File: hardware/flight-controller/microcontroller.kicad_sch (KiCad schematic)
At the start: 40 parts, among them J1 IDC-6, J2 IDC-10, J3 Conn_01x05, SW1 SW_Push, U1 STM32U535RET6, U2 ESP-12E, Y1 8 MHz

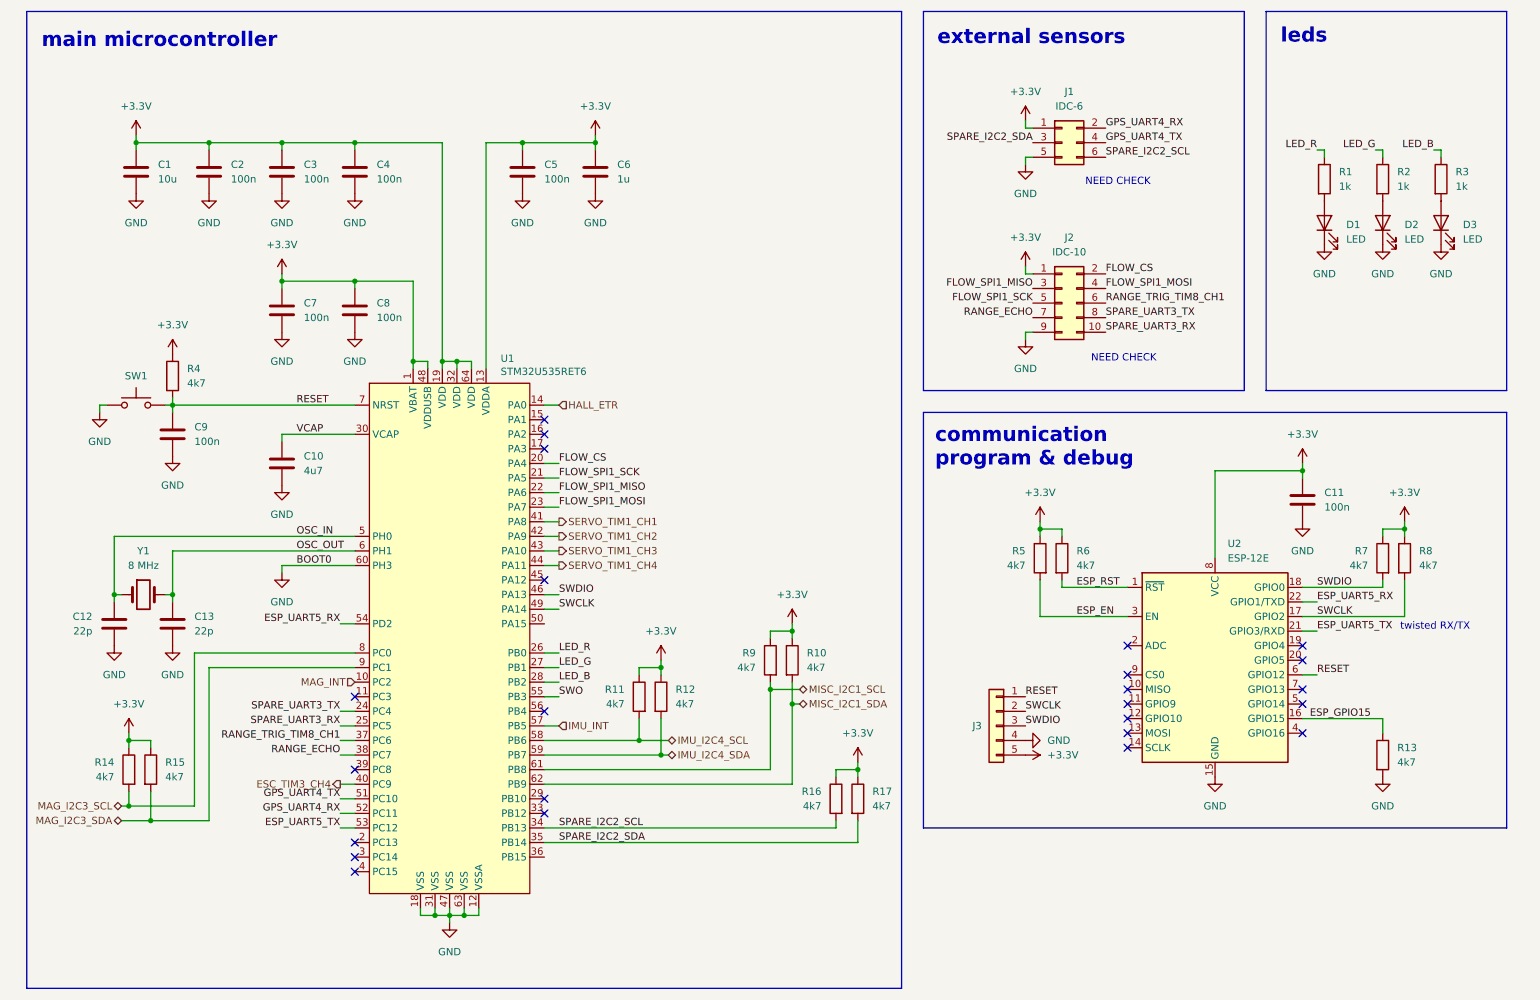
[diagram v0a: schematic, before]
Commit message: sensors, power, actuators, filters
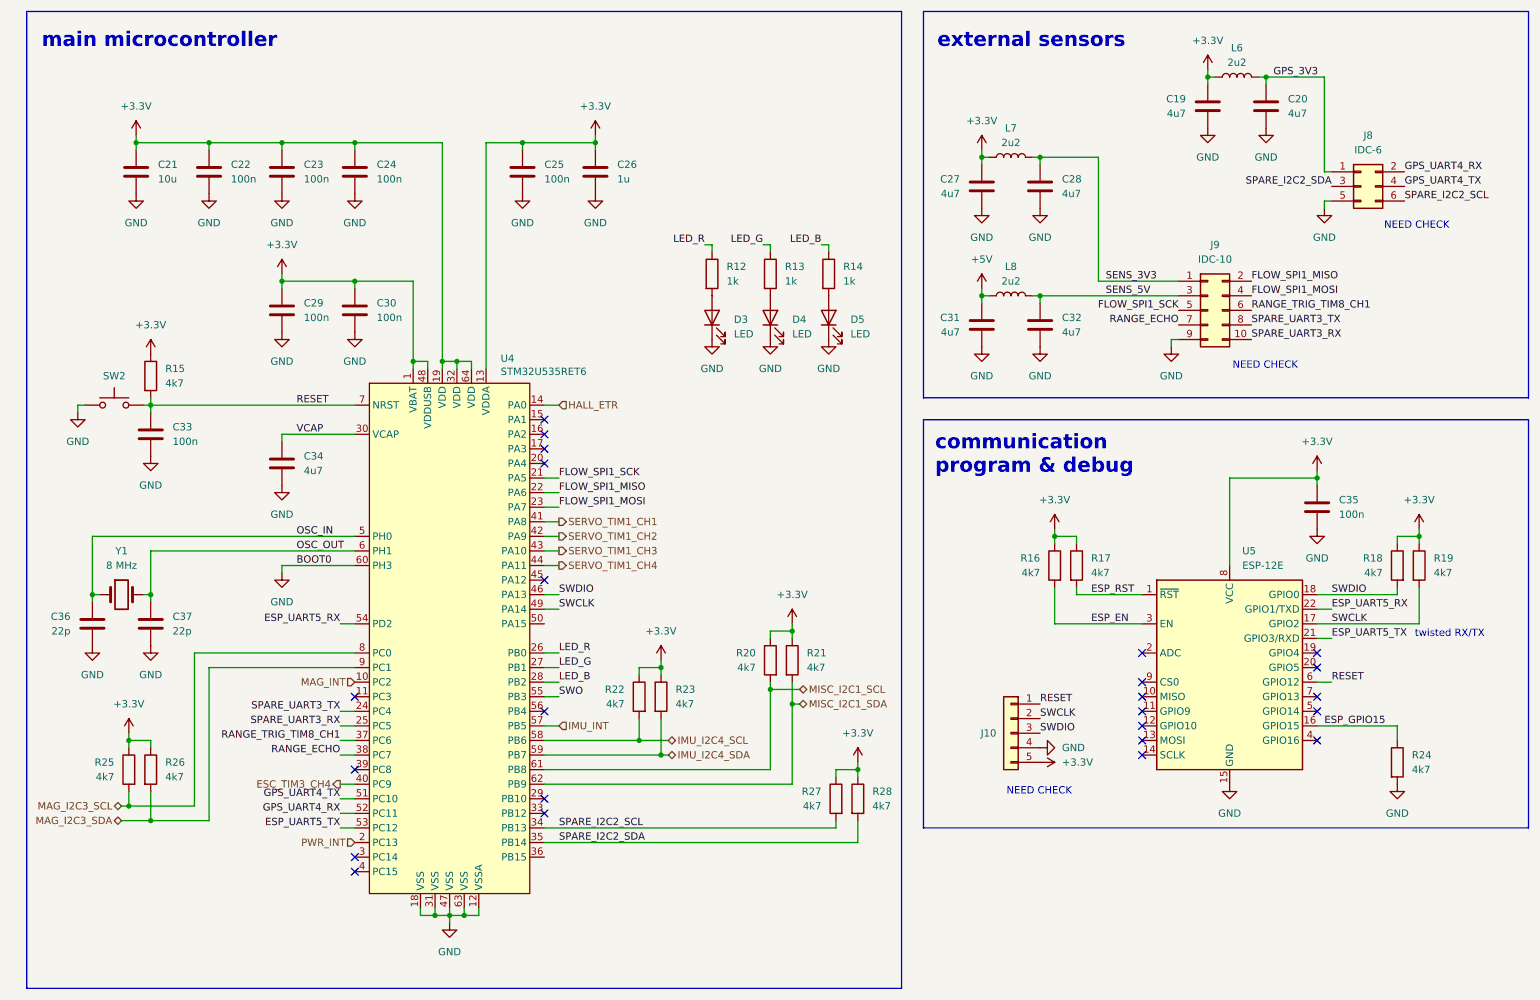
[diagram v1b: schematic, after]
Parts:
- removed C11: 100n, symbol Device:C
- added C19, C20, C27, C28, C31, C32: 4u7, symbol Device:C
- added C35: 100n, symbol Device:C
- added L6, L7, L8: 2u2, symbol Device:L
- renumbered C1 to C21, C2 to C22, C3 to C23, C4 to C24, C5 to C25, C6 to C26, C7 to C29, C8 to C30, C9 to C33, C10 to C34, C12 to C36, C13 to C37, D1 to D3, D2 to D4, D3 to D5, J3 to J10, J1 to J8, J2 to J9, R1 to R12, R2 to R13, R3 to R14, R4 to R15, R5 to R16, R6 to R17, R7 to R18, R8 to R19, R9 to R20, R10 to R21, R11 to R22, R12 to R23, R13 to R24, R14 to R25, R15 to R26, R16 to R27, R17 to R28, SW1 to SW2, U1 to U4, U2 to U5
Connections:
- net +3.3V: now also C19.1, C27.1, C35.1, L6.1, L7.1; no longer J8.1 (Pin_1), J9.1 (Pin_1)
- net FLOW_SPI1_MISO: now also J9.2 (Pin_2); no longer J9.3 (Pin_3)
- net GND: now also C19.2, C20.2, C27.2, C28.2, C31.2, C32.2, C35.2
- net PWR_INT: now reaches U4.2 (PC13)
- net FLOW_CS: no longer names the net of U4.20 (PA4)
- net FLOW_CS: no longer J9.2 (Pin_2)
- new net +5V: C31.1, L8.1
- new net GPS_3V3: C20.1, J8.1 (Pin_1), L6.2
- new net SENS_3V3: C28.1, J9.1 (Pin_1), L7.2
- new net SENS_5V: C32.1, J9.3 (Pin_3), L8.2
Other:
- note removed: "leds"
- moved on the sheet: C33, C36, C37, D3, D4, D5, J10, J8, J9, R12, R13, R14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

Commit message: schematic cleanup
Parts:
- removed C19, C20, C27, C28, C31, C32: 4u7, symbol Device:C
- removed J8: IDC-6, symbol Connector_Generic:Conn_02x03_Odd_Even
- removed J9: IDC-10, symbol Connector_Generic:Conn_02x05_Odd_Even
- removed L6, L7, L8: 2u2, symbol Device:L
- removed R27, R28: 4k7, symbol Device:R
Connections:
- net FLOW_CS: now reaches U4.20 (PA4)
- net ESC_TIM3_CH4 renamed ESC
- net ESP_UART5_RX renamed ESP_RX
- net ESP_UART5_TX renamed ESP_TX
- net FLOW_SPI1_MISO renamed FLOW_MISO
- net FLOW_SPI1_MOSI renamed FLOW_MOSI
- net FLOW_SPI1_SCK renamed FLOW_SCK
- net GPS_UART4_RX renamed GPS_RX
- net GPS_UART4_TX renamed GPS_TX
- net HALL_ETR renamed HALL
- net IMU_I2C4_SCL renamed IMU_SCL
- net IMU_I2C4_SDA renamed IMU_SDA
- net MAG_I2C3_SCL renamed MAG_SCL
- net MAG_I2C3_SDA renamed MAG_SDA
- net MISC_I2C1_SCL renamed MISC_SCL
- net MISC_I2C1_SDA renamed MISC_SDA
- net RANGE_TRIG_TIM8_CH1 renamed RANGE_TRIG
- net SERVO_TIM1_CH1 renamed SERVO1
- net SERVO_TIM1_CH2 renamed SERVO2
- net SERVO_TIM1_CH3 renamed SERVO3
- net SERVO_TIM1_CH4 renamed SERVO4
- net SPARE_I2C2_SCL: no longer names the net of U4.34 (PB13)
- net SPARE_I2C2_SDA: no longer names the net of U4.35 (PB14)
- net SPARE_UART3_RX: no longer names the net of U4.25 (PC5)
- net SPARE_UART3_TX renamed FLOW_INT
- no-connect marks 24 -> 28
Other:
- note added: "twisted"
- note removed: "external sensors"
- note removed: "twisted RX/TX"
- moved on the sheet: C35, J10, R16, R17, R18, R19, R24, U5

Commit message: still working
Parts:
- removed R12, R13, R14: 1k, symbol Device:R
- removed R22, R23, R25, R26: 4k7, symbol Device:R
- added R18, R19, R20: 1k, Resistor_SMD:R_0603_1608Metric, symbol Device:R
- C12: renamed from C22; footprint (none) -> Capacitor_SMD:C_0603_1608Metric
- C13: renamed from C23; footprint (none) -> Capacitor_SMD:C_0603_1608Metric
- C14: renamed from C24; footprint (none) -> Capacitor_SMD:C_0603_1608Metric
- C15: renamed from C25; footprint (none) -> Capacitor_SMD:C_0603_1608Metric
- C17: renamed from C35; footprint (none) -> Capacitor_SMD:C_0603_1608Metric
- C18: renamed from C29; footprint (none) -> Capacitor_SMD:C_0603_1608Metric
- C19: renamed from C30; footprint (none) -> Capacitor_SMD:C_0603_1608Metric
- C20: renamed from C33; footprint (none) -> Capacitor_SMD:C_0603_1608Metric
- C22: renamed from C36; footprint (none) -> Capacitor_SMD:C_0603_1608Metric
- C23: renamed from C37; footprint (none) -> Capacitor_SMD:C_0603_1608Metric
- D3: value LED -> RED; footprint (none) -> LED_SMD:LED_0603_1608Metric
- D4: value LED -> GREEN; footprint (none) -> LED_SMD:LED_0603_1608Metric
- D5: value LED -> BLUE; footprint (none) -> LED_SMD:LED_0603_1608Metric
- J2: renamed from J10; footprint (none) -> Connector_PinHeader_2.54mm:PinHeader_1x05_P2.54mm_Vertical
- R12: renamed from R18; footprint (none) -> Resistor_SMD:R_0603_1608Metric
- R13: renamed from R19; footprint (none) -> Resistor_SMD:R_0603_1608Metric
- R14: renamed from R16; footprint (none) -> Resistor_SMD:R_0603_1608Metric
- R15: renamed from R17; footprint (none) -> Resistor_SMD:R_0603_1608Metric
- R16: renamed from R15; footprint (none) -> Resistor_SMD:R_0603_1608Metric
- R17: renamed from R24; footprint (none) -> Resistor_SMD:R_0603_1608Metric
- R21: renamed from R20; footprint (none) -> Resistor_SMD:R_0603_1608Metric
- R22: renamed from R21; footprint (none) -> Resistor_SMD:R_0603_1608Metric
- Y1: footprint (none) -> Crystal:Crystal_SMD_5032-2Pin_5.0x3.2mm
- renumbered C21 to C11, C26 to C16, C34 to C21, U5 to U4, U4 to U5
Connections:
- net LED_B: now also R20.1
- net LED_G: now also R19.1
- net LED_R: now also R18.1
- net PWR_INT: now also U5.38 (PC7); no longer U5.2 (PC13)
- net RANGE_ECHO: now also U5.36 (PB15); no longer U5.38 (PC7)
- net at D3.2 (A): now also R18.2
- net at D5.2 (A): now also R20.2
- net at D4.2 (A): now also R19.2
- net SPARE_PA1: now reaches U5.15 (PA1)
- net SPARE_PA2: now reaches U5.16 (PA2)
- net SPARE_PA3: now reaches U5.17 (PA3)
- net SPARE_UART_RX: now reaches U5.25 (PC5)
- net SPARE_UART_TX: now reaches U5.29 (PB10)
- net LOAD_DOUT: now reaches U5.3 (PC14)
- net SPARE_I2C_SCL: now reaches U5.34 (PB13)
- net SPARE_I2C_SDA: now reaches U5.35 (PB14)
- net LOAD_SCK: now reaches U5.4 (PC15)
- net ESP_RX renamed ESP_TXD
- net ESP_TX renamed ESP_RXD
- net GPS_RX renamed GPS_TXD
- net GPS_TX renamed GPS_RXD
- net HALL renamed TACH
- net SWO: no longer names the net of U5.55 (PB3)
- new net LOAD_RATE: U5.2 (PC13)
- no-connect marks 28 -> 19
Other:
- note added: "leds"
- note added: "to ST-LINK (just in case)"
- note removed: "NEED CHECK"
- note removed: "twisted"
- moved on the sheet: C17, J2, R12, R13, R14, R15, R17, R21, R22, U4

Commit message: clean footprints
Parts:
- U5: footprint Package_QFP:LQFP-64_10x10mm_P0.5mm -> goose:stm32u535ret6
- Y1: value 8 MHz -> 8MHz; footprint Crystal:Crystal_SMD_5032-2Pin_5.0x3.2mm -> goose:oscillator_5032_2
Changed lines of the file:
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@@
 			)
 		)
-		(property "Value" "8 MHz"
+		(property "Value" "8MHz"
 			(at 36.83 116.84 0)
 			(effects
@@
 			)
 		)
-		(property "Footprint" "Crystal:Crystal_SMD_5032-2Pin_5.0x3.2mm"
+		(property "Footprint" "goose:oscillator_5032_2"
 			(at 36.83 121.92 0)
 			(effects
@@
 			)
 		)
-		(property "Footprint" "Package_QFP:LQFP-64_10x10mm_P0.5mm"
+		(property "Footprint" "goose:stm32u535ret6"
 			(at 93.98 127 0)
 			(effects

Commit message: more clean footprints
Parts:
- U4: footprint RF_Module:ESP-12E -> goose:esp12e
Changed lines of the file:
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@@
 			)
 		)
-		(property "Footprint" "RF_Module:ESP-12E"
+		(property "Footprint" "goose:esp12e"
 			(at 229.87 82.55 0)
 			(effects

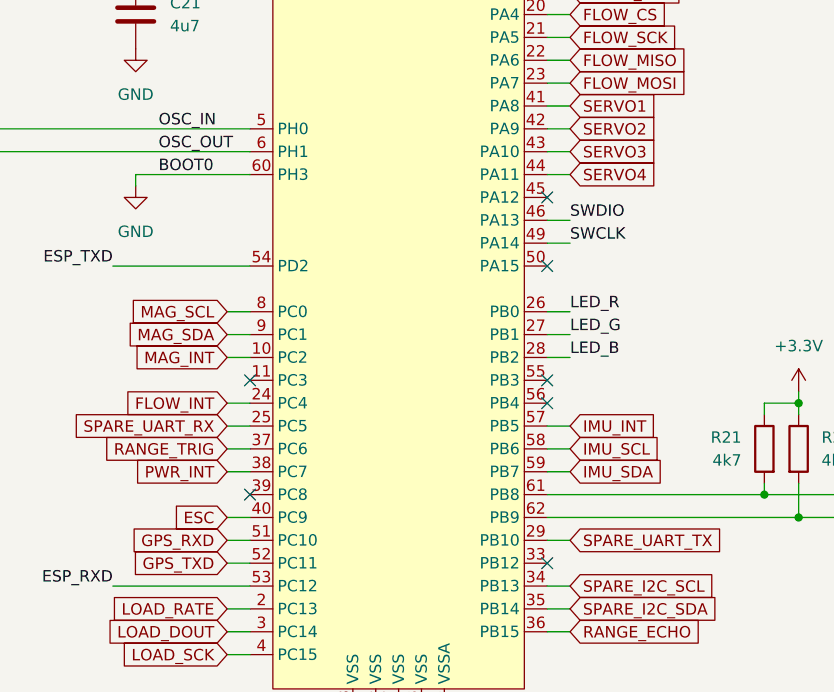
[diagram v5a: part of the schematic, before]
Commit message: clean footprints
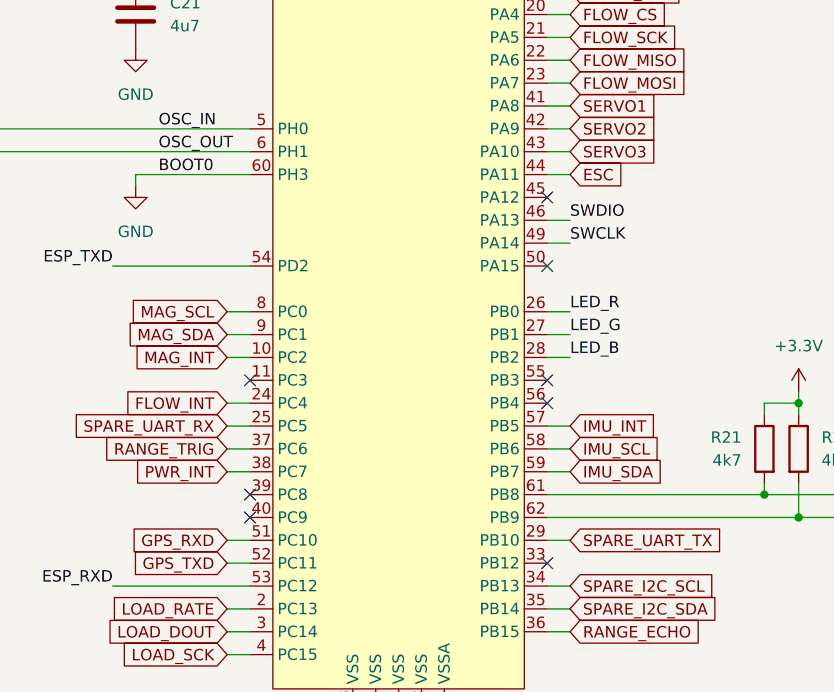
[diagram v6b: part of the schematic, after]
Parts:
- C11, C16, C21: footprint (none) -> Capacitor_SMD:C_0603_1608Metric
- J2: footprint Connector_PinHeader_2.54mm:PinHeader_1x05_P2.54mm_Vertical -> goose:header_1x5_not_used
- U4: footprint goose:esp12e -> goose:ESP-12E
- U5: footprint goose:stm32u535ret6 -> goose:STM32U535RET6
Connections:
- net SERVO4 is gone; now on net ESC: U5.44 (PA11)
- net ESC: no longer U5.40 (PC9)
- no-connect marks 19 -> 20
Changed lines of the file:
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@@
 	)
 	(no_connect
+		(at 77.47 154.94)
+	)
+	(no_connect
 		(at 110.49 127)
 	)
@@
 	(wire
 		(pts
-			(xy 74.93 154.94) (xy 77.47 154.94)
-		)
-		(stroke
-			(width 0)
-			(type default)
-		)
-	)
-	(wire
-		(pts
 			(xy 138.43 142.24) (xy 138.43 143.51)
 		)
@@
 		)
 	)
-	(global_label "SERVO4"
-		(shape input)
-		(at 113.03 116.84 0)
-		(fields_autoplaced yes)
-		(effects
-			(font
-				(size 1.27 1.27)
-			)
-			(justify left)
-		)
-		(property "Intersheetrefs" "${INTERSHEET_REFS}"
-			(at 123.2723 116.84 0)
-			(effects
-				(font
-					(size 1.27 1.27)
-				)
-				(justify left)
-				(hide yes)
-			)
-		)
-	)
 	(global_label "SPARE_I2C_SCL"
 		(shape input)
@@
 		)
 	)
+	(global_label "ESC"
+		(shape input)
+		(at 113.03 116.84 0)
+		(fields_autoplaced yes)
+		(effects
+			(font
+				(size 1.27 1.27)
+			)
+			(justify left)
+		)
+		(property "Intersheetrefs" "${INTERSHEET_REFS}"
+			(at 119.6437 116.84 0)
+			(effects
+				(font
+					(size 1.27 1.27)
+				)
+				(justify left)
+				(hide yes)
+			)
+		)
+	)
 	(global_label "FLOW_SCK"
 		(shape input)
@@
 		)
 	)
-	(global_label "ESC"
-		(shape input)
-		(at 74.93 154.94 180)
-		(fields_autoplaced yes)
-		(effects
-			(font
-				(size 1.27 1.27)
-			)
-			(justify right)
-		)
-		(property "Intersheetrefs" "${INTERSHEET_REFS}"
-			(at 68.3163 154.94 0)
-			(effects
-				(font
-					(size 1.27 1.27)
-				)
-				(justify right)
-				(hide yes)
-			)
-		)
-	)
 	(global_label "SPARE_I2C_SDA"
 		(shape input)
@@
 			)
 		)
-		(property "Footprint" ""
+		(property "Footprint" "Capacitor_SMD:C_0603_1608Metric"
 			(at 120.3452 52.07 0)
 			(effects
@@
 			)
 		)
-		(property "Footprint" "Connector_PinHeader_2.54mm:PinHeader_1x05_P2.54mm_Vertical"
+		(property "Footprint" "goose:header_1x5_not_used"
 			(at 187.96 97.79 0)
 			(effects
@@
 			)
 		)
-		(property "Footprint" "goose:esp12e"
+		(property "Footprint" "goose:ESP-12E"
 			(at 229.87 82.55 0)
 			(effects
@@
 			)
 		)
-		(property "Footprint" ""
+		(property "Footprint" "Capacitor_SMD:C_0603_1608Metric"
 			(at 40.3352 52.07 0)
 			(effects
@@
 			)
 		)
-		(property "Footprint" ""
+		(property "Footprint" "Capacitor_SMD:C_0603_1608Metric"
 			(at 65.7352 102.87 0)
 			(effects
@@
 			)
 		)
-		(property "Footprint" "goose:stm32u535ret6"
+		(property "Footprint" "goose:STM32U535RET6"
 			(at 93.98 127 0)
 			(effects

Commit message: clean models
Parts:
- C22: renamed from C21; value 4u7 -> 4.7u
- R11: renamed from R12; value 4k7 -> 4.7k
- R12: renamed from R13; value 4k7 -> 4.7k
- R13: renamed from R14; value 4k7 -> 4.7k
- R14: renamed from R15; value 4k7 -> 4.7k
- R15: renamed from R16; value 4k7 -> 4.7k
- R16: renamed from R17; value 4k7 -> 4.7k
- R20: renamed from R21; value 4k7 -> 4.7k
- R21: renamed from R22; value 4k7 -> 4.7k
- renumbered C11 to C12, C12 to C13, C13 to C14, C14 to C15, C15 to C16, C16 to C17, C17 to C18, C18 to C19, C19 to C20, C20 to C21, C22 to C23, C23 to C24, R18 to R17, R19 to R18, R20 to R19
